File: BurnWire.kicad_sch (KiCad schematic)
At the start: 11 parts, among them U1 ADP2303ARDZ

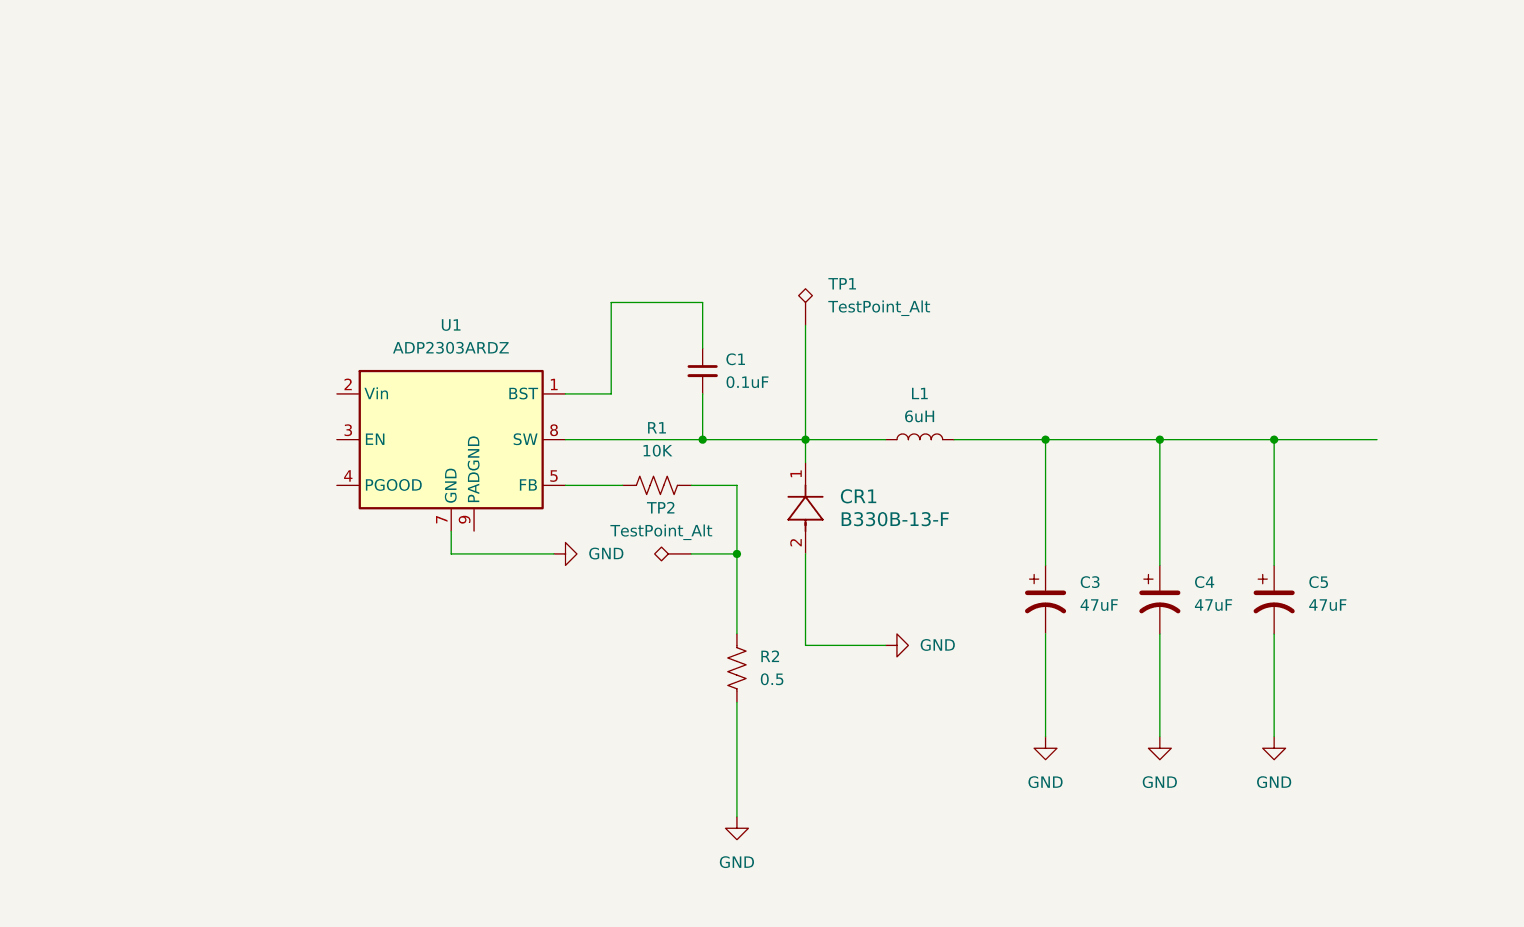
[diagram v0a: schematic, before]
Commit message: completed schematic, added most footprints
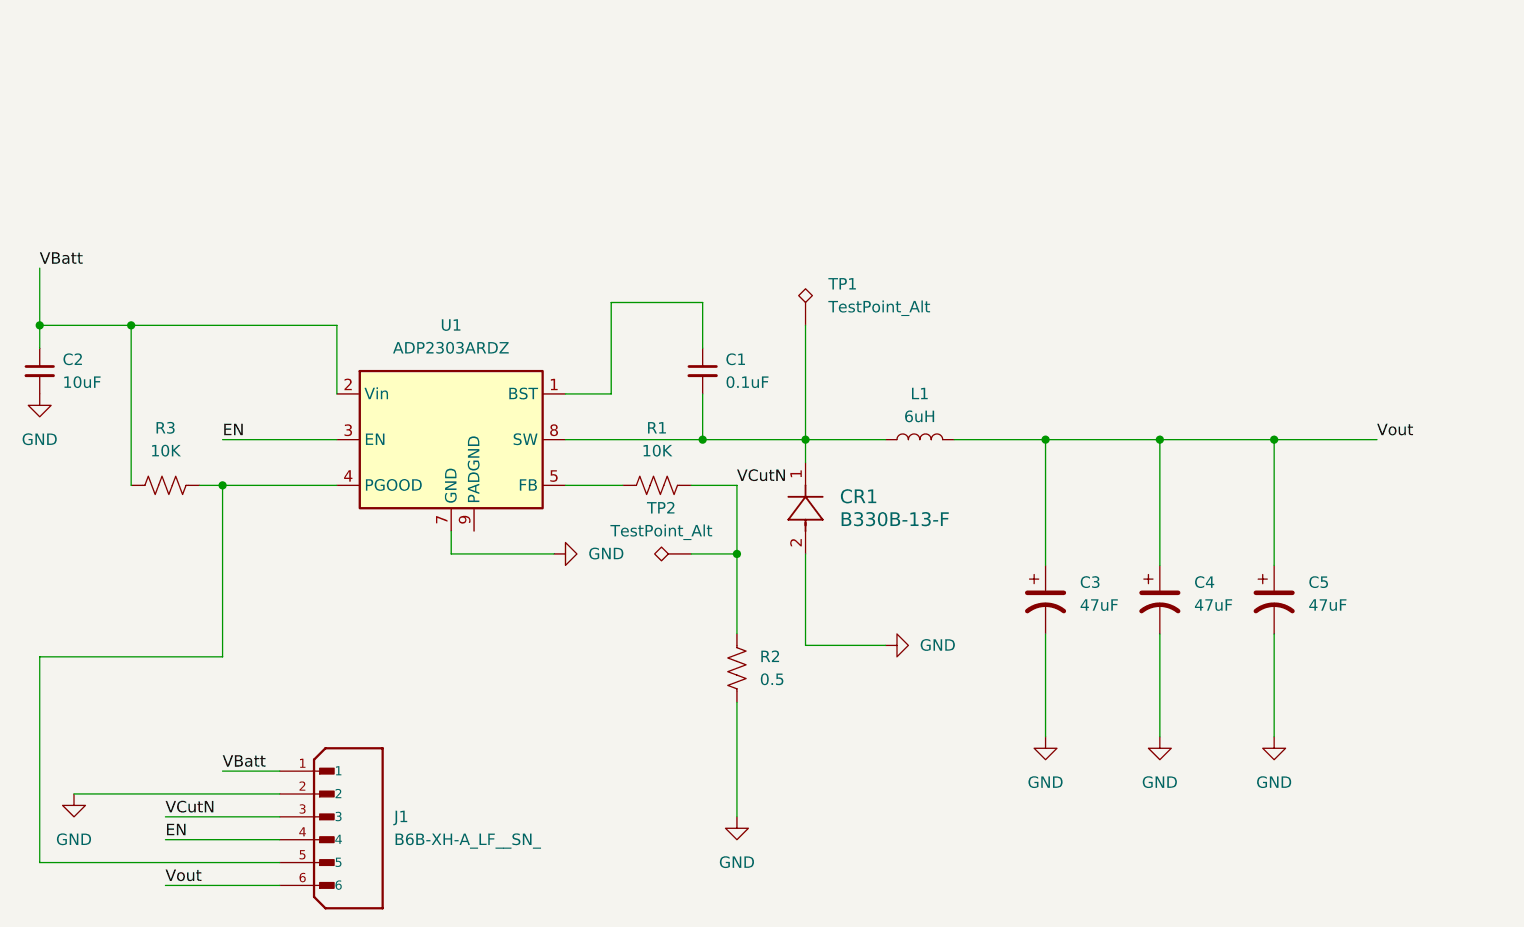
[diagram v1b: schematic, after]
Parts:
- added C2: 10uF, Capacitor_THT:CP_Axial_L10.0mm_D4.5mm_P15.00mm_Horizontal, symbol Device:C_Small
- added J1: B6B-XH-A_LF__SN_, B6B-XH-A_LF__SN_:JST_B6B-XH-A_LF__SN_, symbol B6B-XH-A_LF__SN_:B6B-XH-A_LF__SN_
- added R3: 10K, Resistor_THT:R_Axial_DIN0204_L3.6mm_D1.6mm_P5.08mm_Horizontal, symbol Device:R_US
- C1, C3, C4, C5: footprint (none) -> Capacitor_THT:CP_Axial_L10.0mm_D4.5mm_P15.00mm_Horizontal
- CR1: footprint CR_SMB_320-345BE_DIO -> (none)
- R1: footprint (none) -> Resistor_THT:R_Axial_DIN0204_L3.6mm_D1.6mm_P2.54mm_Vertical
- R2: footprint (none) -> Resistor_THT:R_Axial_DIN0204_L3.6mm_D1.6mm_P5.08mm_Horizontal
- TP1, TP2: footprint (none) -> TestPoint:TestPoint_2Pads_Pitch5.08mm_Drill1.3mm
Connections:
- net GND: now also C2.2, J1.2
- net VCutN: now reaches R1.2, R2.1, TP2.1
- net VCutN: now also J1.3
- net Vout: now reaches C3.1, C4.1, C5.1, L1.2
- net Vout: now also J1.6
- net VBatt: now reaches U1.2 (Vin)
- net VBatt: now also C2.1, J1.1, R3.1
- net EN: now reaches U1.3 (EN)
- net EN: now also J1.4
- net at U1.4 (PGOOD): now also J1.5, R3.2

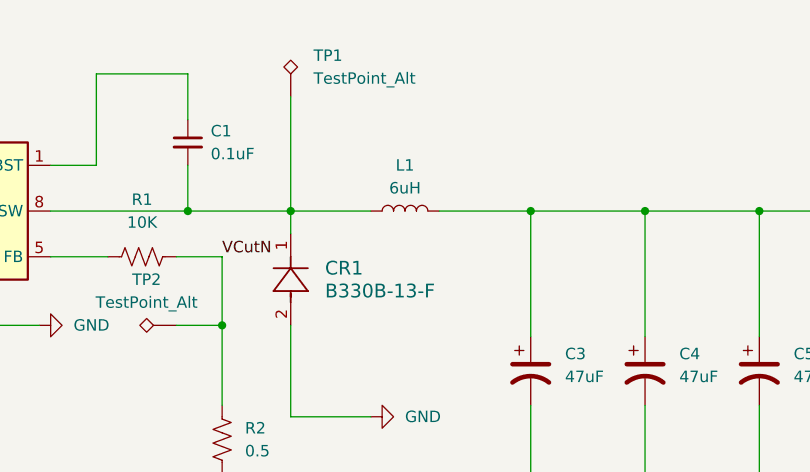
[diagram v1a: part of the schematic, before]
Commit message: Added footprint libraries, reorganized imported components, Assigned footprints
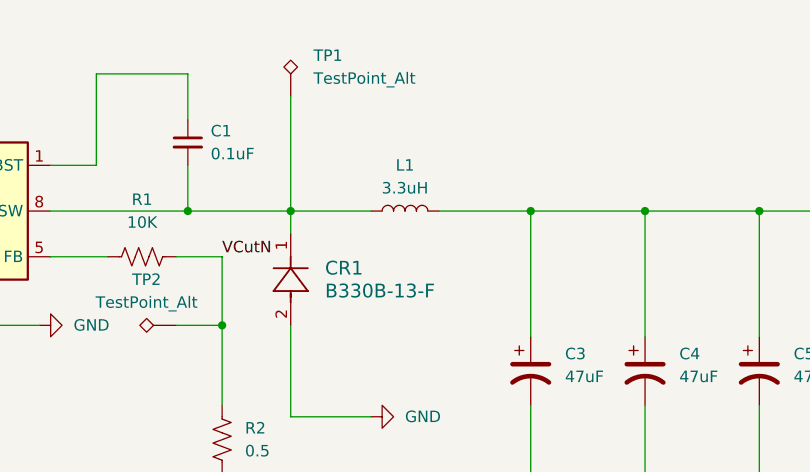
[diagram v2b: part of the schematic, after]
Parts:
- CR1: footprint (none) -> imported_footprints:CR_SMB_320-345BE_DIO
- J1: footprint B6B-XH-A_LF__SN_:JST_B6B-XH-A_LF__SN_ -> imported_footprints:JST_B6B-XH-A_LF__SN_
- L1: value 6uH -> 3.3uH; footprint (none) -> imported_footprints:IND_NLV32T_TDK
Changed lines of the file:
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@@
 			)
 		)
-		(property "Footprint" ""
+		(property "Footprint" "imported_footprints:CR_SMB_320-345BE_DIO"
 			(at 151.13 95.25 0)
 			(effects
@@
 			)
 		)
-		(property "Footprint" "B6B-XH-A_LF__SN_:JST_B6B-XH-A_LF__SN_"
+		(property "Footprint" "imported_footprints:JST_B6B-XH-A_LF__SN_"
 			(at 100.33 124.46 0)
 			(effects
@@
 			)
 		)
-		(property "Value" "6uH"
+		(property "Value" "3.3uH"
 			(at 163.83 80.01 90)
 			(effects
@@
 			)
 		)
-		(property "Footprint" ""
+		(property "Footprint" "imported_footprints:IND_NLV32T_TDK"
 			(at 163.83 82.55 0)
 			(effects

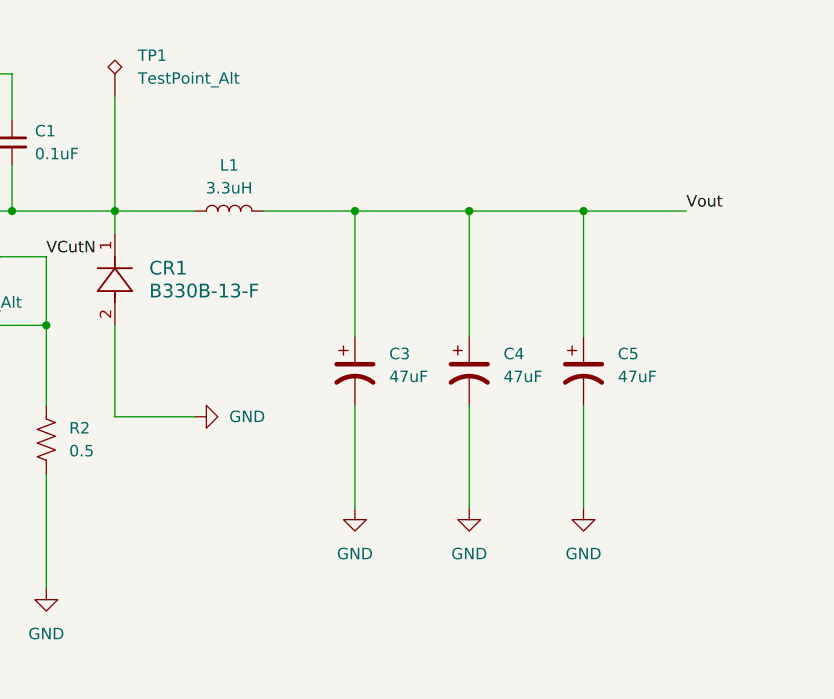
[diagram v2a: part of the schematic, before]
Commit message: imported more footprints, completed layout
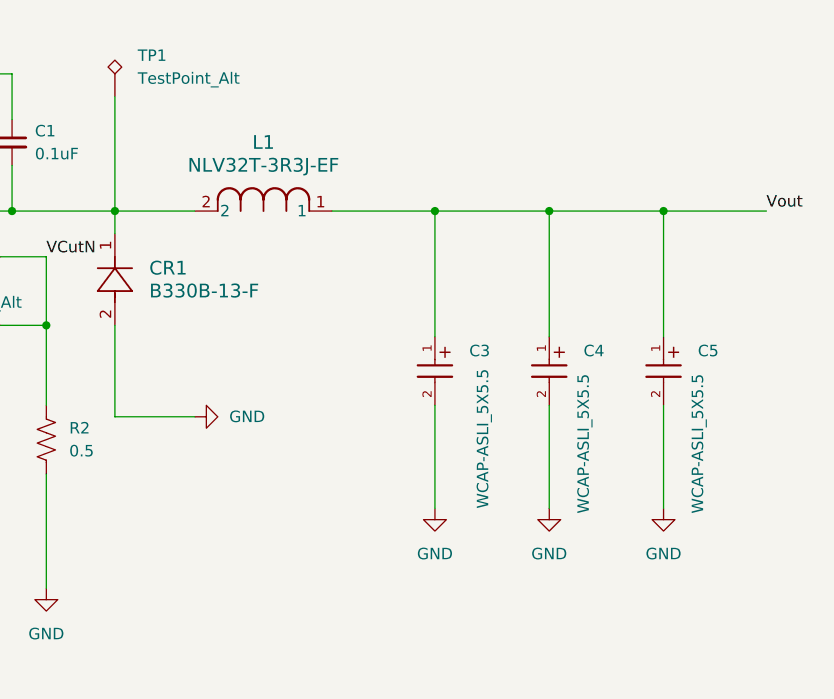
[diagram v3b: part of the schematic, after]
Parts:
- removed C3, C4, C5: 47uF, Capacitor_THT:CP_Axial_L10.0mm_D4.5mm_P15.00mm_Horizontal, symbol Device:C_Polarized_US
- removed L1: 3.3uH, imported_footprints:IND_NLV32T_TDK, symbol Device:L
- added C3, C4, C5: WCAP-ASLI_5X5.5, WCAP-ASLI:WCAP-ASLI_5X5.5_DXL_, symbol WCAP-ASLI_5X5.5:WCAP-ASLI_5X5.5
- added L1: NLV32T-3R3J-EF, imported_footprints:IND_NLV32T_TDK, symbol 2025-11-02_20-08-03:NLV32T-3R3J-EF
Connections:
- net GND: now also C3.2, C4.2, C5.2
- net Vout: now also C3.1, C4.1, C5.1, L1.1
- net at C1.2, CR1.1, TP1.1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: now also L1.2

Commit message: done
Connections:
- net GND: now also U1.9 (PADGND)
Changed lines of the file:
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@@
+	)
+	(junction
+		(at 114.3 95.25)
+		(diameter 0)
+		(color 0 0 0 0)
 	)
 	(junction
@@
 	(wire
 		(pts
-			(xy 123.19 95.25) (xy 111.76 95.25)
+			(xy 123.19 95.25) (xy 114.3 95.25)
 		)
 		(stroke
@@
 	(wire
 		(pts
+			(xy 114.3 92.71) (xy 114.3 95.25)
+		)
+		(stroke
+			(width 0)
+			(type default)
+		)
+	)
+	(wire
+		(pts
 			(xy 138.43 95.25) (xy 143.51 95.25)
 		)
@@
 		)
 		(stroke
+			(width 0)
+			(type default)
+		)
+	)
+	(wire
+		(pts
+			(xy 114.3 95.25) (xy 111.76 95.25)
+		)
+		(stroke

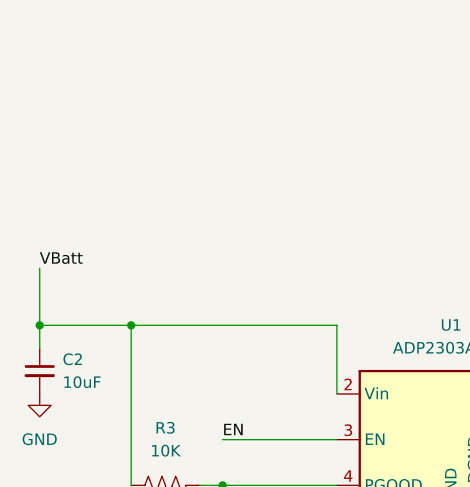
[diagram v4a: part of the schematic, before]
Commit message: started one layer
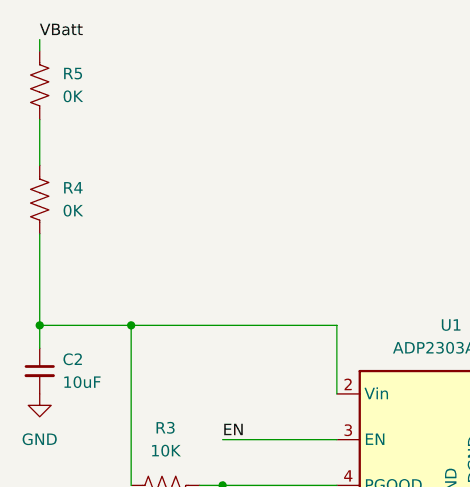
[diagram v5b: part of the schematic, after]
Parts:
- added R4, R5: 0K, Resistor_THT:R_Axial_DIN0204_L3.6mm_D1.6mm_P5.08mm_Horizontal, symbol Device:R_US
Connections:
- net VBatt: now also R5.2; no longer C2.1, R3.1, U1.2 (Vin)
- new net: R4.2, R5.1
- new net: C2.1, R3.1, R4.1, U1.2 (Vin)
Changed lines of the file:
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@@
+	(wire
+		(pts
+			(xy 66.04 38.1) (xy 66.04 39.37)
+		)
+		(stroke
+			(width 0)
+			(type default)
+		)
+	)
 	(wire
 		(pts
@@
 	(wire
 		(pts
+			(xy 66.04 59.69) (xy 66.04 69.85)
+		)
+		(stroke
+			(width 0)
+			(type default)
+		)
+	)
+	(wire
+		(pts
 			(xy 151.13 95.25) (xy 151.13 105.41)
 		)
@@
 	(wire
 		(pts
+			(xy 66.04 46.99) (xy 66.04 52.07)
+		)
+		(stroke
+			(width 0)
+			(type default)
+		)
+	)
+	(wire
+		(pts
 			(xy 143.51 95.25) (xy 143.51 87.63)
 		)
@@
 		(pts
 			(xy 186.69 82.55) (xy 199.39 82.55)
-		)
-		(stroke
-			(width 0)
-			(type default)
-		)
-	)
-	(wire
-		(pts
-			(xy 66.04 63.5) (xy 66.04 69.85)
 		)
 		(stroke
@@
 		)
 	)
-	(label "VBatt"
-		(at 66.04 63.5 0)
-		(effects
-			(font
-				(size 1.27 1.27)
-			)
-			(justify left bottom)
-		)
-	)
 	(label "EN"
 		(at 80.01 127 0)
@@
 	(label "VCutN"
 		(at 80.01 124.46 0)
+		(effects
+			(font
+				(size 1.27 1.27)
+			)
+			(justify left bottom)
+		)
+	)
+	(label "VBatt"
+		(at 66.04 38.1 0)
 		(effects
 			(font
@@
 	)
 	(symbol
+		(lib_id "Device:R_US")
+		(at 66.04 43.18 180)
+		(unit 1)
+		(exclude_from_sim no)
+		(in_bom yes)
+		(on_board yes)
+		(dnp no)
+		(fields_autoplaced yes)
+		(property "Reference" "R5"
+			(at 68.58 41.9099 0)
+			(effects
+				(font
+					(size 1.27 1.27)
+				)
+				(justify right)
+			)
+		)
+		(property "Value" "0K"
+			(at 68.58 44.4499 0)
+			(effects
+				(font
+					(size 1.27 1.27)
+				)
+				(justify right)
+			)
+		)
+		(property "Footprint" "Resistor_THT:R_Axial_DIN0204_L3.6mm_D1.6mm_P5.08mm_Horizontal"
+			(at 65.024 42.926 90)
+			(effects
+				(font
+					(size 1.27 1.27)
+				)
+				(hide yes)
+			)
+		)
+		(property "Datasheet" "~"
+			(at 66.04 43.18 0)
+			(effects
+				(font
+					(size 1.27 1.27)
+				)
+				(hide yes)
+			)
+		)
+		(property "Description" "Resistor, US symbol"
+			(at 66.04 43.18 0)
+			(effects
+				(font
+					(size 1.27 1.27)
+				)
+				(hide yes)
+			)
+		)
+		(pin "1"
+		)
+		(pin "2"
+		)
+		(instances
+			(project "BurnWire"
+				(path "/f35490b1-adcb-463e-9dac-9bc4e552c2ef"
+					(reference "R5")
+					(unit 1)
+				)
+			)
+		)
+	)
+	(symbol
 		(lib_id "power:GND")
 		(at 212.09 115.57 0)
@@
 					(unit 1)
 				)
+			)
+		)
+	)
+	(symbol
+		(lib_id "Device:R_US")
+		(at 66.04 55.88 180)
+		(unit 1)
+		(exclude_from_sim no)
+		(in_bom yes)
+		(on_board yes)
+		(dnp no)
+		(fields_autoplaced yes)
+		(property "Reference" "R4"
+			(at 68.58 54.6099 0)
+			(effects
+				(font
+					(size 1.27 1.27)
+				)
+				(justify right)
+			)
+		)
+		(property "Value" "0K"
+			(at 68.58 57.1499 0)
+			(effects
+				(font
+					(size 1.27 1.27)
+				)
+				(justify right)
+			)
+		)
+		(property "Footprint" "Resistor_THT:R_Axial_DIN0204_L3.6mm_D1.6mm_P5.08mm_Horizontal"
+			(at 65.024 55.626 90)
+			(effects
+				(font
+					(size 1.27 1.27)
+				)
+				(hide yes)
+			)
+		)
+		(property "Datasheet" "~"
+			(at 66.04 55.88 0)
+			(effects
+				(font
+					(size 1.27 1.27)
+				)
+				(hide yes)
+			)
+		)
+		(property "Description" "Resistor, US symbol"
+			(at 66.04 55.88 0)
+			(effects
+				(font
+					(size 1.27 1.27)
+				)
+				(hide yes)
+			)
+		)
+		(pin "1"
+		)
+		(pin "2"
+		)
+		(instances
+			(project "BurnWire"
+				(path "/f35490b1-adcb-463e-9dac-9bc4e552c2ef"
+					(reference "R4")
+					(unit 1)
+				)
